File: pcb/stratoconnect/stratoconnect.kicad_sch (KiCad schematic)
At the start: 37 parts, among them J1 Conn_Coaxial, J2 Conn_02x03_Odd_Even, J3 Conn_01x05_Male, J4 Conn_01x02_Male, J5 Conn_01x03_Male, SW1 SW_SPST, SW2 SW_SPST, U1 RF4463f30, U2 ATmega328PB-A, U3 TPS61022RWU, Y1 CSTNE16M0V530000R0

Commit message: build out the VQFN7-7 footbring for the boost converter
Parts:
- H3: footprint (none) -> MountingHole:MountingHole_3.2mm_M3_Pad_Via
- U3: footprint Package_SON:WSON-8-1EP_2x2mm_P0.5mm_EP0.9x1.6mm -> Package_DFN_QFN:VDFN-7_2.1x2.1mm
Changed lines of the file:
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@@
       (effects (font (size 1.27 1.27)) (justify left) hide)
     )
-    (property "Footprint" "" (id 2) (at 125.095 22.86 0)
+    (property "Footprint" "MountingHole:MountingHole_3.2mm_M3_Pad_Via" (id 2) (at 125.095 22.86 0)
       (effects (font (size 1.27 1.27)) hide)
     )
@@
       (effects (font (size 1.27 1.27)) (justify left))
     )
-    (property "Footprint" "Package_SON:WSON-8-1EP_2x2mm_P0.5mm_EP0.9x1.6mm" (id 2) (at 232.41 69.215 0)
+    (property "Footprint" "Package_DFN_QFN:VDFN-7_2.1x2.1mm" (id 2) (at 232.41 69.215 0)
       (effects (font (size 1.27 1.27)) hide)
     )
@@
     )
     (path "/82b188f6-6403-4e6c-9961-757480bdd7fa"
-      (reference "U3") (unit 1) (value "TPS61022RWU") (footprint "Package_SON:WSON-8-1EP_2x2mm_P0.5mm_EP0.9x1.6mm")
+      (reference "U3") (unit 1) (value "TPS61022RWU") (footprint "Package_DFN_QFN:VDFN-7_2.1x2.1mm")
     )
     (path "/325e0de3-190a-4e12-9c8e-cac7e8ed9534"

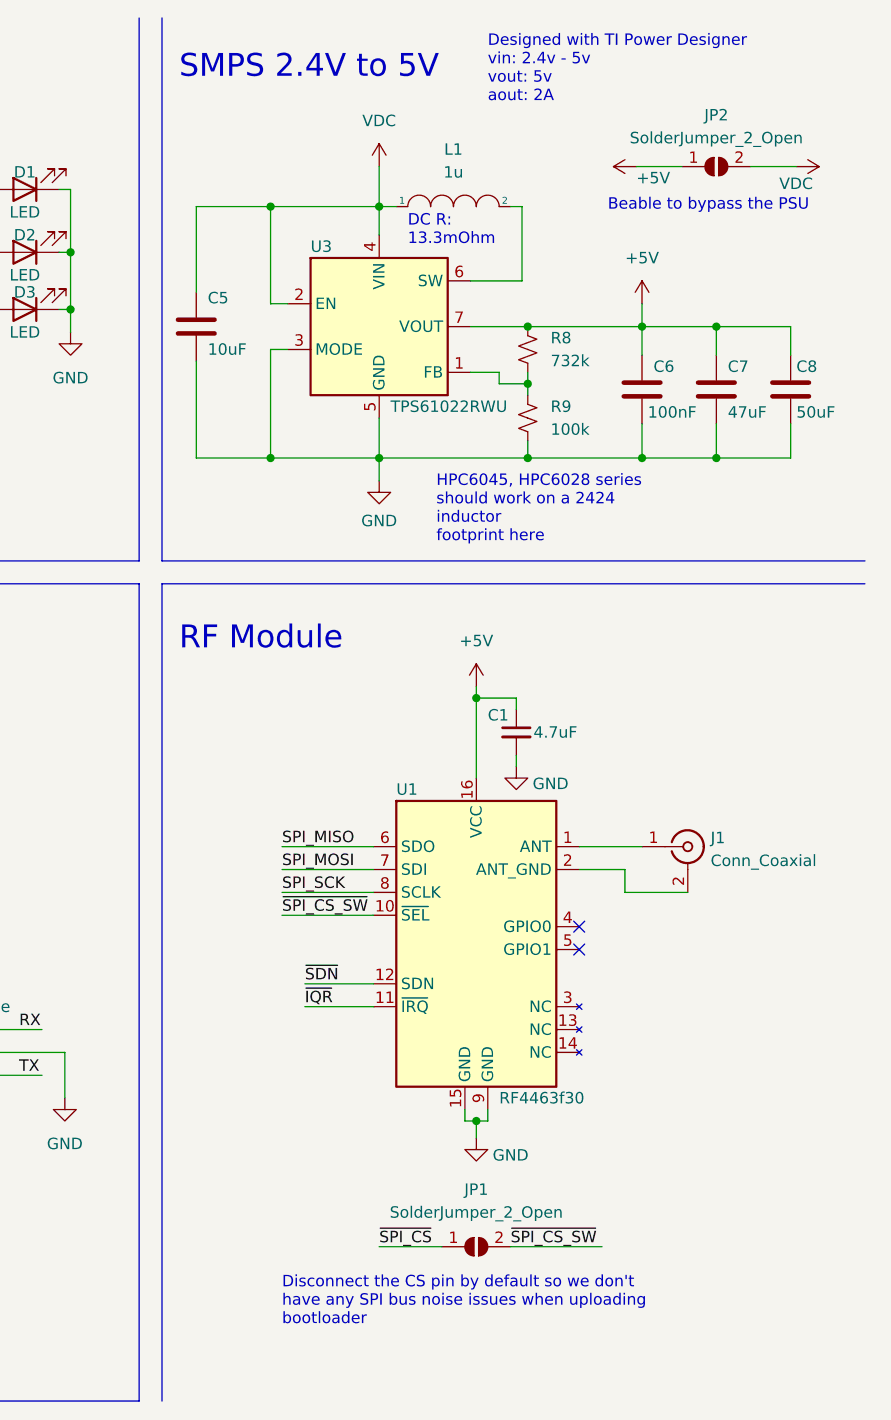
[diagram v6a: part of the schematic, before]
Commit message: update schematic to add mroe room for the smps
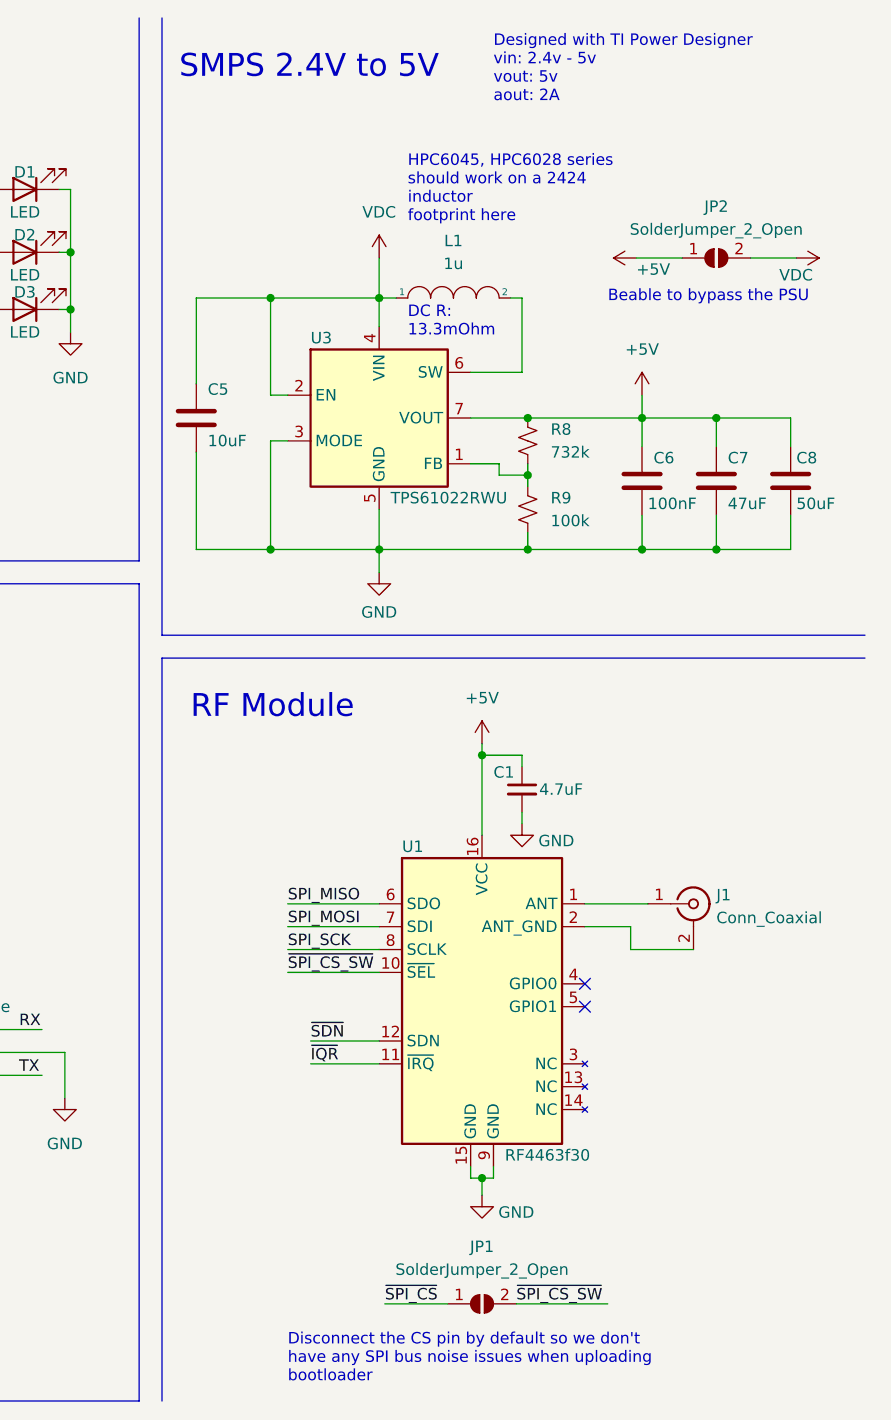
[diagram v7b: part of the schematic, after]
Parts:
- J1: footprint Connector_Coaxial:SMA_Molex_73251-2120_EdgeMount_Horizontal -> Connector_Coaxial:SMA_Molex_73251-2200_Horizontal
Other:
- moved on the sheet: C1, C5, C6, C7, C8, J1, JP1, JP2, L1, R8, R9, U1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

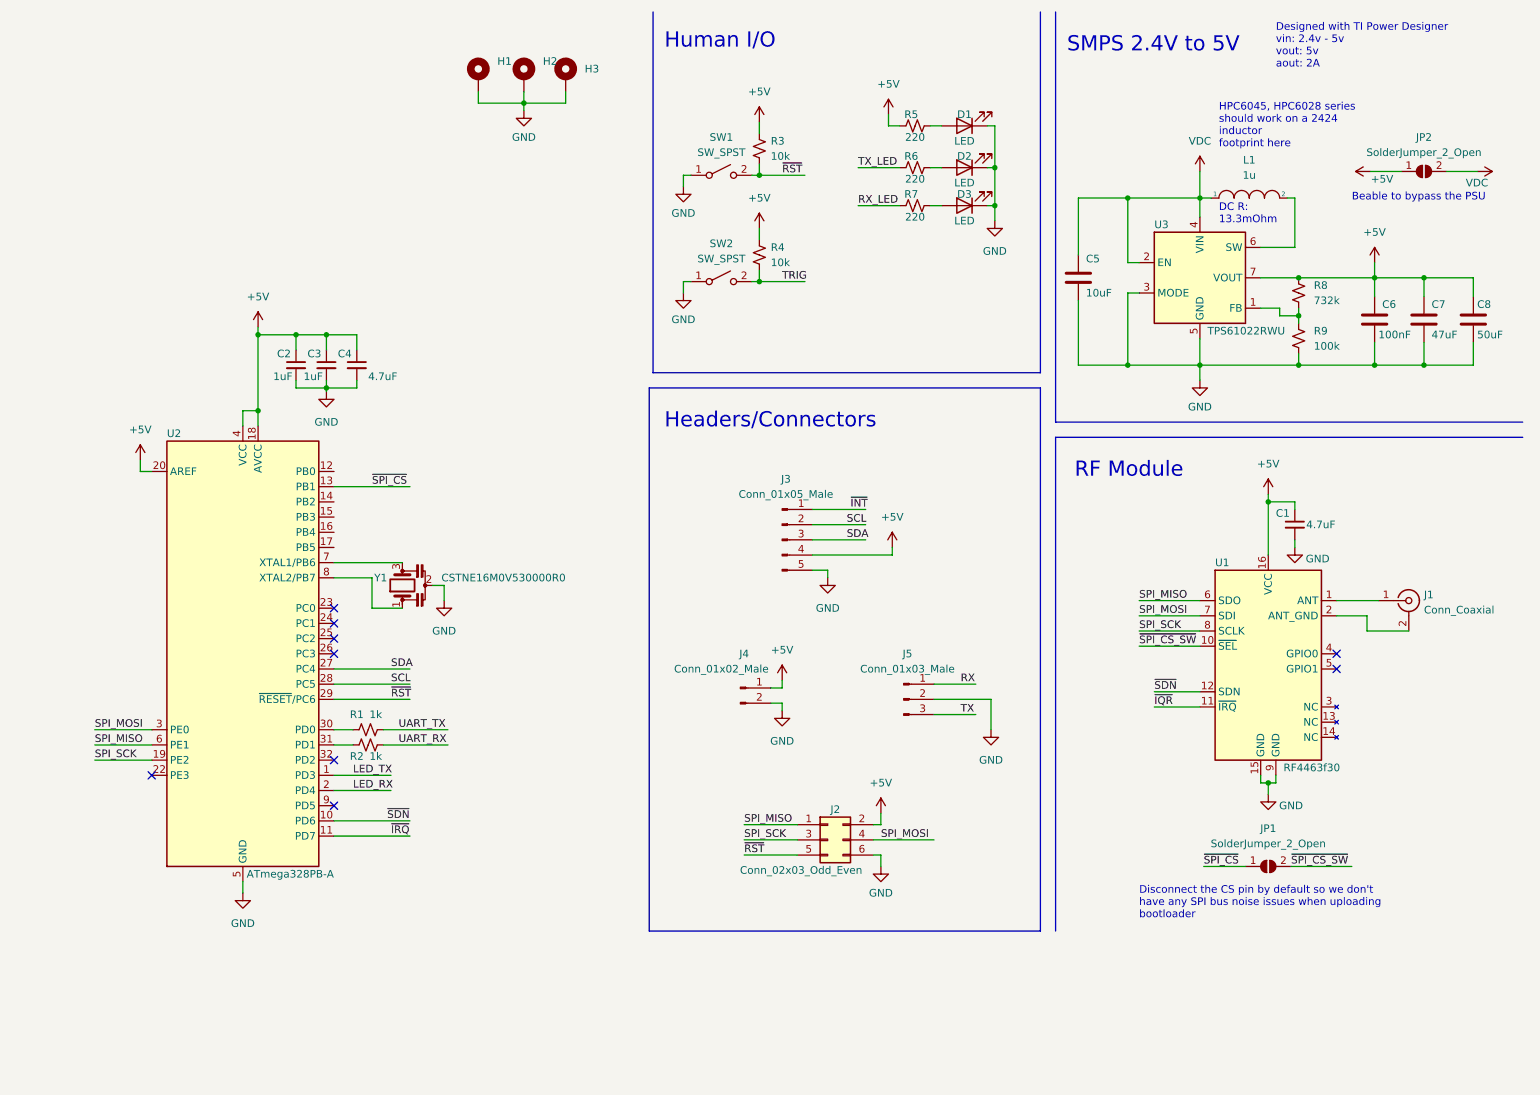
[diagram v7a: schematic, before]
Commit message: finish routing the smps, need to extend the footprint pads for the rf module
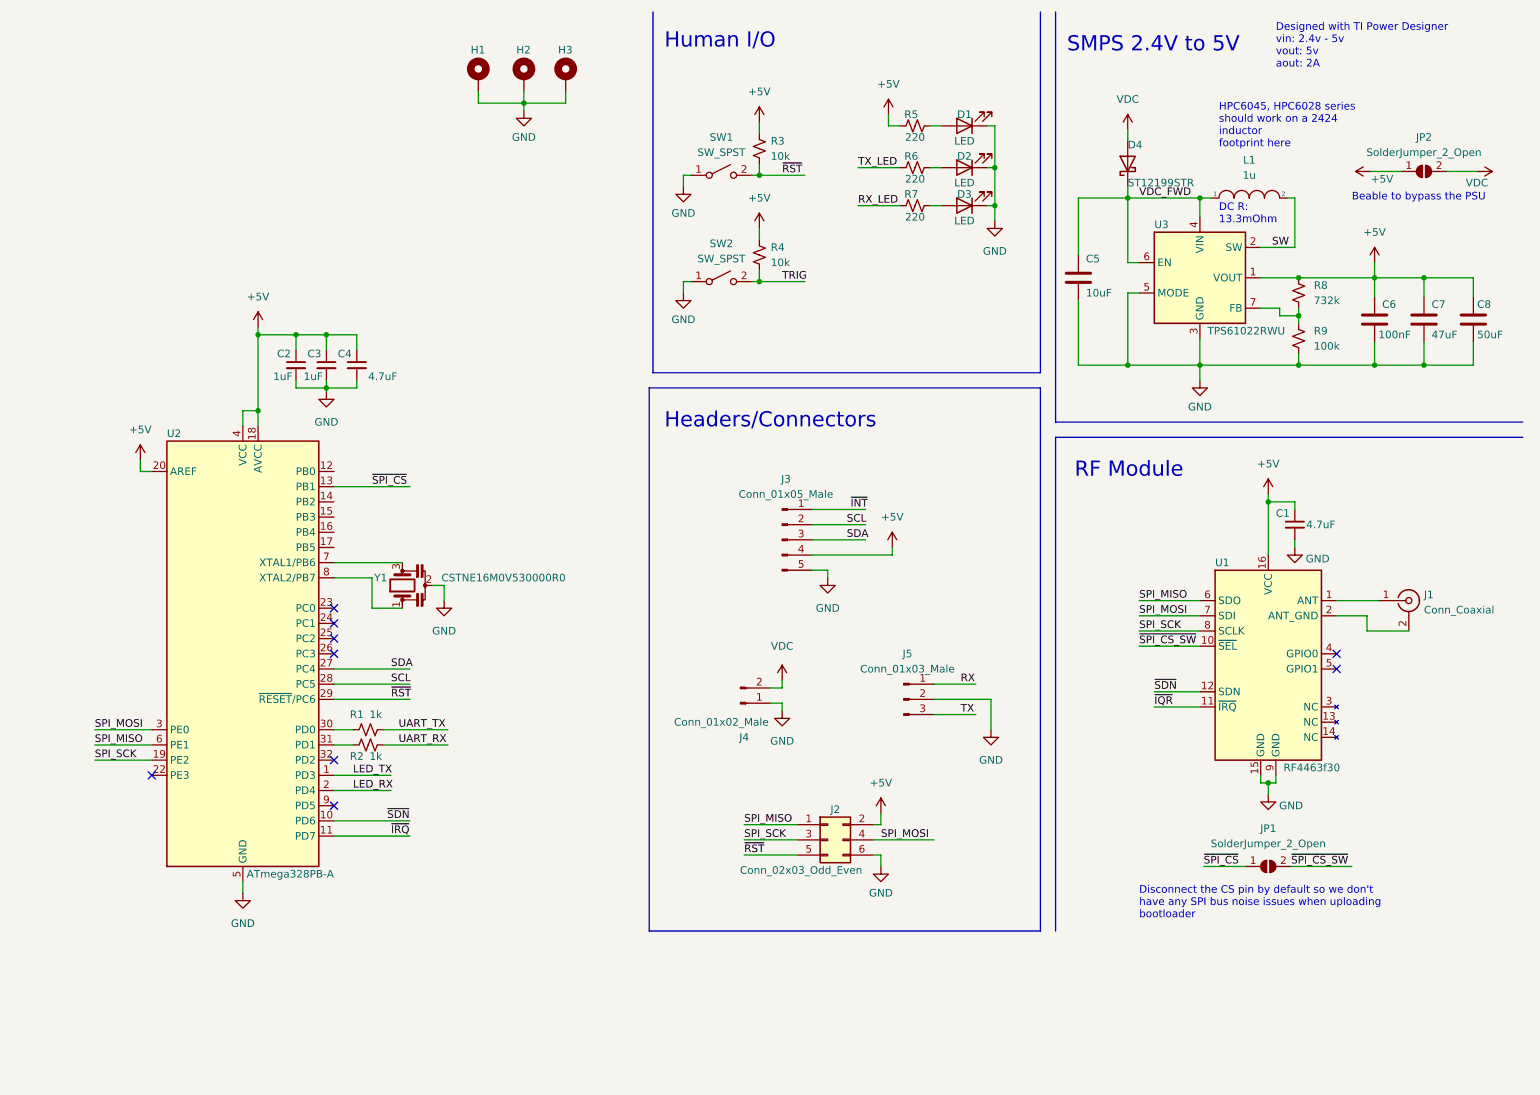
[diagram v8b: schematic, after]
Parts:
- added D4: ST12199STR, Kevin_Lutzer_Lbr:Diode-TO-277B, symbol Kevin_Lutzer_Lbr:ST12199STR
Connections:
- net +5V: now also U3.1 (VOUT); no longer J4.1 (Pin_1), U3.7 (VOUT)
- net GND: now also J4.1 (Pin_1); no longer J4.2 (Pin_2)
- net VDC: now also J4.2 (Pin_2), D4.2 (A); no longer C5.1, L1.1, U3.2 (EN), U3.4 (VIN)
- net at R8.2, R9.1: now also U3.7 (FB); no longer U3.1 (FB)
- net SW: now reaches L1.2
- net SW: now also U3.2 (SW); no longer U3.6 (SW)
- new net VDC_FWD: C5.1, D4.1 (K), L1.1, U3.4 (VIN), U3.6 (EN)
